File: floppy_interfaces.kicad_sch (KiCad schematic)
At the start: 24 parts, among them J13 Conn_01x04_Male, J14 Conn_02x17_Odd_Even, J16 Conn_01x04_Male, J6 SDF-60J for IEC 1541 serial p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, U1 74HC245, U2 74HC245, U22 74LS06N, U3 74HC245

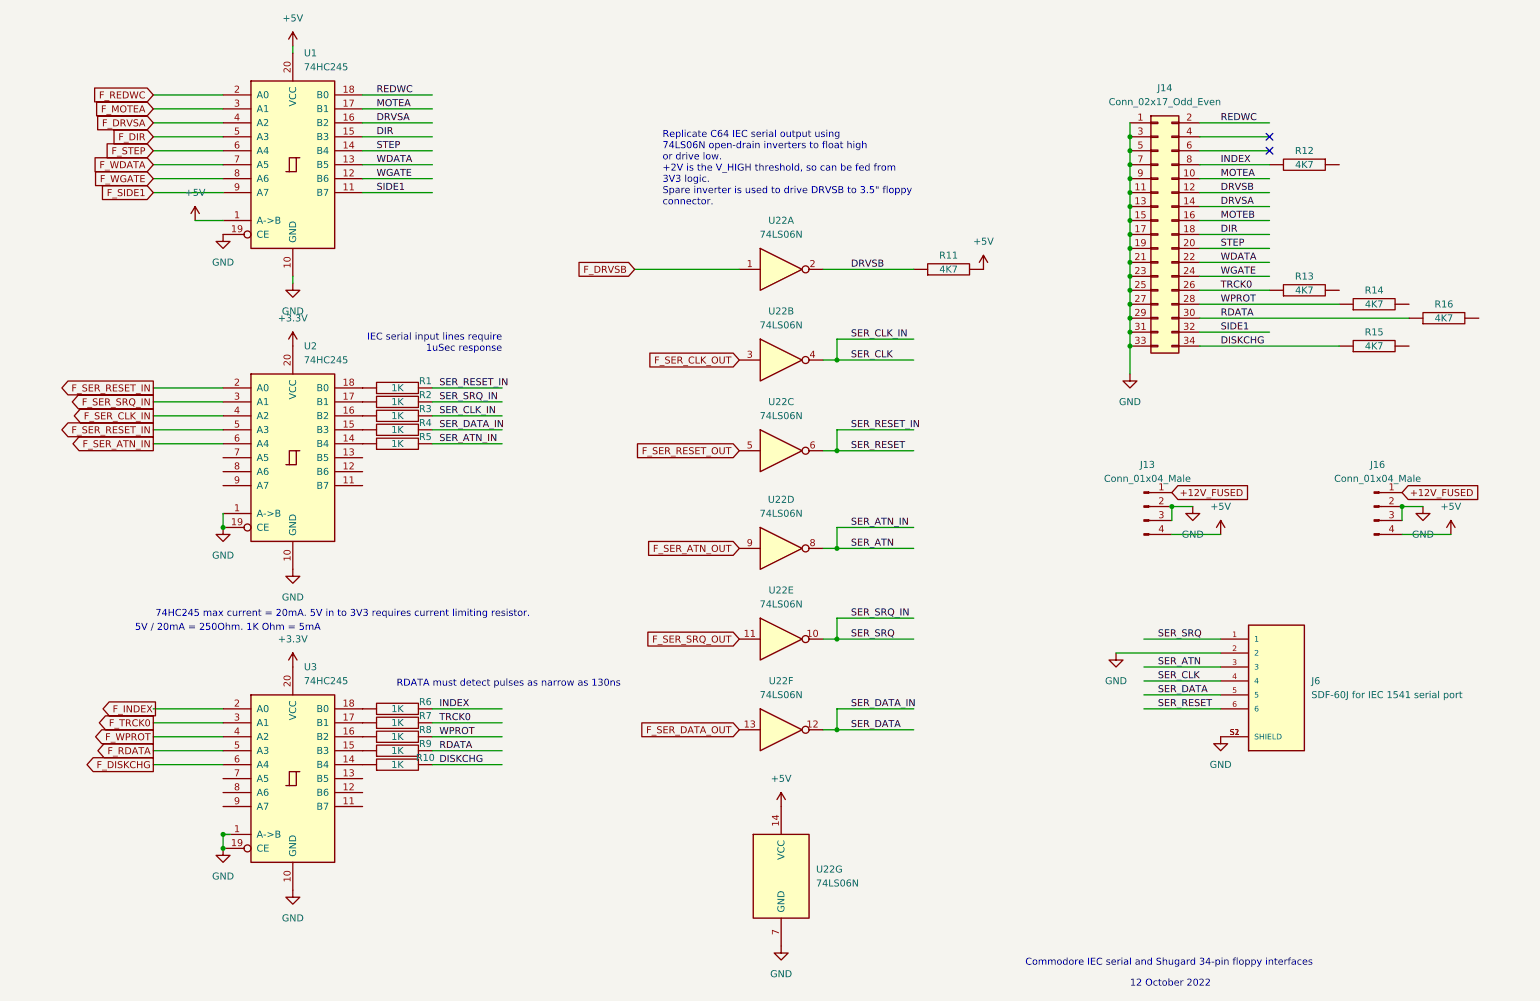
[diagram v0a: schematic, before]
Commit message: rework floppy buffers to use mux bus
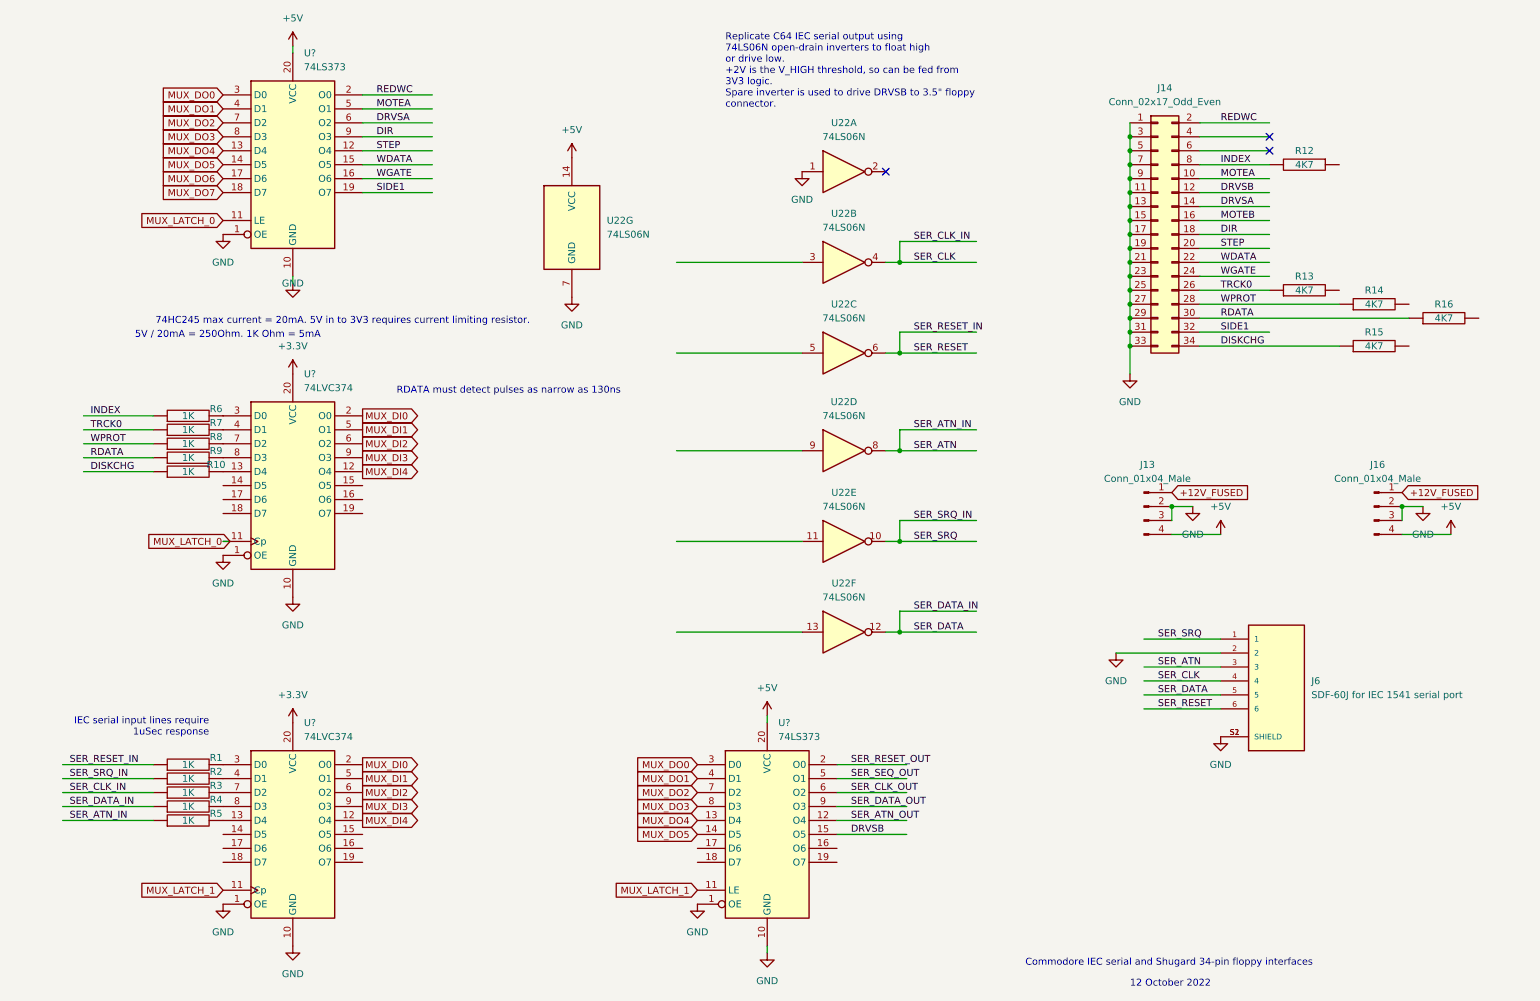
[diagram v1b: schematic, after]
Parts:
- removed R11: 4K7, Resistor_THT:R_Box_L8.4mm_W2.5mm_P5.08mm, symbol pspice:R
- removed U1, U2, U3: 74HC245, Package_DIP:DIP-20_W7.62mm, symbol 74xx:74HC245
- added U? (x2): 74LS373, symbol 74xx:74LS373
- added U? (x2): 74LVC374, Package_DIP:DIP-20_W7.62mm, symbol 74xx:74HC374
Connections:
- net F_DRVSB is gone; now on net GND: U22.1
- net +3V3: now also U?.20 (VCC), U?.20 (VCC)
- net +5V: now also U?.20 (VCC), U?.20 (VCC)
- net DIR: now also U?.9 (O3)
- net DISKCHG: now also R10.1; no longer R10.2
- net DRVSA: now also U?.6 (O2)
- net DRVSB: now also U?.15 (O5); no longer U22.2
- net GND: now also U?.1 (OE), U?.1 (OE), U?.1 (OE), U?.1 (OE), U?.10 (GND), U?.10 (GND), U?.10 (GND), U?.10 (GND)
- net INDEX: now also R6.1; no longer R6.2
- net MOTEA: now also U?.5 (O1)
- net RDATA: now also R9.1; no longer R9.2
- net REDWC: now also U?.2 (O0)
- net SER_ATN: now also R5.1; no longer R5.2
- net SER_CLK: now also R3.1; no longer R3.2
- net SER_DATA: now also R4.1; no longer R4.2
- net SER_RESET: now also R1.1; no longer R1.2
- net SER_SRQ: now also R2.1; no longer R2.2
- net SIDE1: now also U?.19 (O7)
- net STEP: now also U?.12 (O4)
- net TRCK0: now also R7.1; no longer R7.2
- net WDATA: now also U?.15 (O5)
- net WGATE: now also U?.16 (O6)
- net WPROT: now also R8.1; no longer R8.2
- net F_SER_ATN_OUT: no longer names the net of U22.9
- net F_SER_CLK_OUT: no longer names the net of U22.3
- net F_SER_DATA_OUT: no longer names the net of U22.13
- net F_SER_RESET_OUT: no longer names the net of U22.5
- net F_SER_SRQ_OUT: no longer names the net of U22.11
- new net: R2.2, U?.4 (D1)
- new net: R8.2, U?.7 (D2)
- new net: R7.2, U?.4 (D1)
- new net: R1.2, U?.3 (D0)
- new net: R5.2, U?.13 (D4)
- new net: R3.2, U?.7 (D2)
- new net: R4.2, U?.8 (D3)
- new net: R9.2, U?.8 (D3)
- new net: R10.2, U?.13 (D4)
- new net: R6.2, U?.3 (D0)
- new net MUX_DI0: U?.2 (O0), U?.2 (O0)
- new net MUX_DI1: U?.5 (O1), U?.5 (O1)
- new net MUX_DI2: U?.6 (O2), U?.6 (O2)
- new net MUX_DI3: U?.9 (O3), U?.9 (O3)
- new net MUX_DI4: U?.12 (O4), U?.12 (O4)
- new net MUX_DO0: U?.3 (D0), U?.3 (D0)
- new net MUX_DO1: U?.4 (D1), U?.4 (D1)
- new net MUX_DO2: U?.7 (D2), U?.7 (D2)
- new net MUX_DO3: U?.8 (D3), U?.8 (D3)
- new net MUX_DO4: U?.13 (D4), U?.13 (D4)
- new net MUX_DO5: U?.14 (D5), U?.14 (D5)
- new net MUX_DO6: U?.17 (D6)
- new net MUX_DO7: U?.18 (D7)
- new net MUX_LATCH_0: U?.11 (Cp), U?.11 (LE)
- new net MUX_LATCH_1: U?.11 (Cp), U?.11 (LE)
- new net SER_ATN_OUT: U?.12 (O4)
- new net SER_CLK_OUT: U?.6 (O2)
- new net SER_DATA_OUT: U?.9 (O3)
- new net SER_RESET_OUT: U?.2 (O0)
- new net SER_SEQ_OUT: U?.5 (O1)
- no-connect marks 2 -> 3
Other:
- moved on the sheet: R1, R10, R2, R3, R4, R5, R6, R7, R8, R9, U22A, U22B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

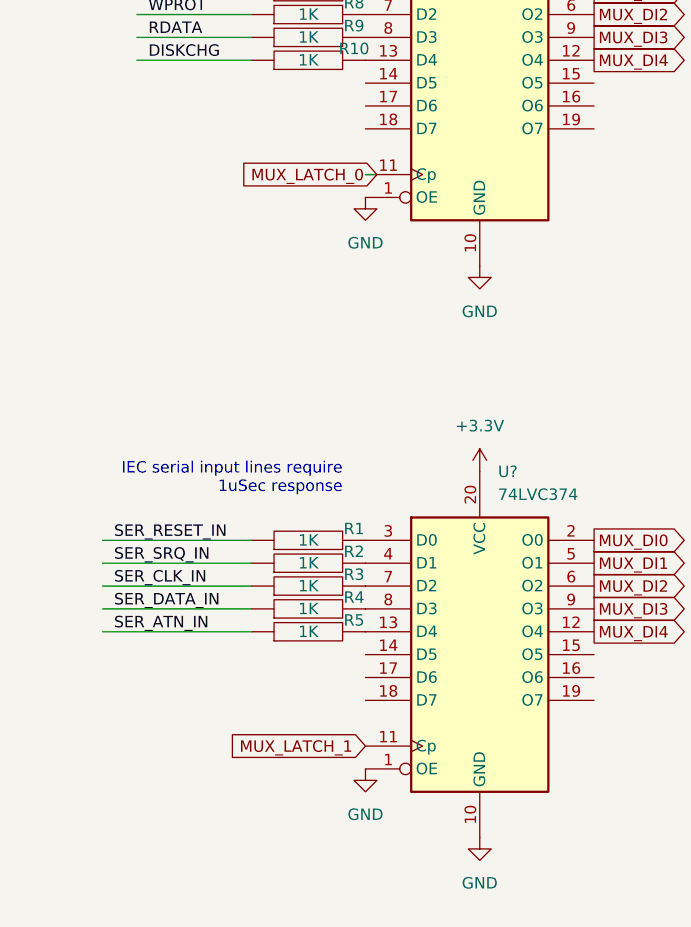
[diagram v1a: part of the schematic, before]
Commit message: add inverting mux to allow use of 74LVC374 as tristate buffer
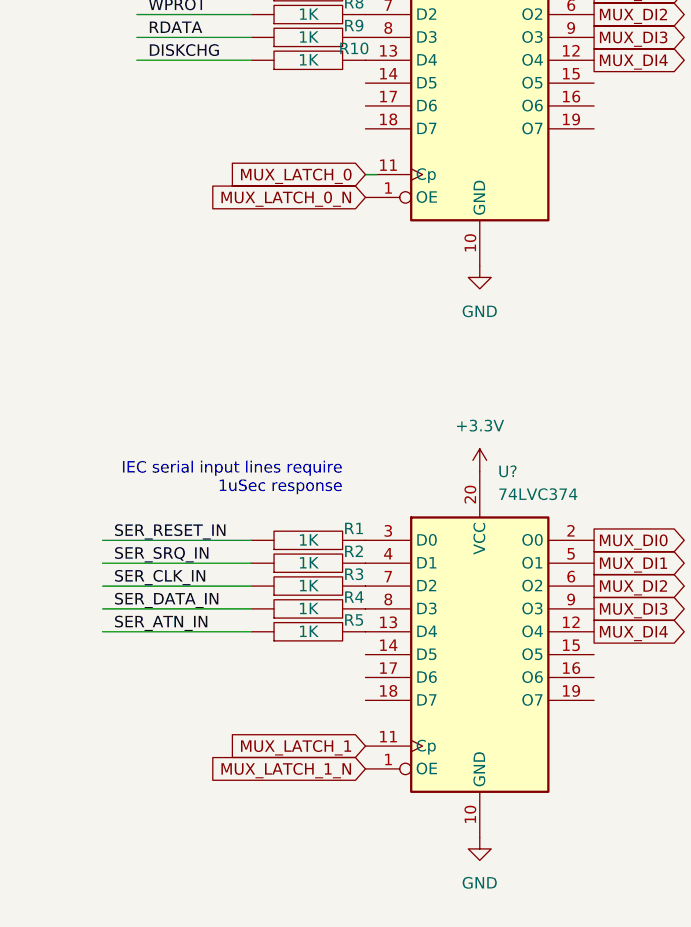
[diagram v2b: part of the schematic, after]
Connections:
- net GND: no longer U?.1 (OE), U?.1 (OE)
- new net MUX_LATCH_0_N: U?.1 (OE)
- new net MUX_LATCH_1_N: U?.1 (OE)
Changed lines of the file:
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@@
     )
   )
-  (global_label "MUX_LATCH_0" (shape input) (at 45.72 113.03 180) (fields_autoplaced)
-    (effects (font (size 1.27 1.27)) (justify right))
-    (property "Intersheet References" "${INTERSHEET_REFS}" (id 0) (at 30.4859 112.9506 0)
+  (global_label "MUX_LATCH_0" (shape input) (at 44.45 113.03 180) (fields_autoplaced)
+    (effects (font (size 1.27 1.27)) (justify right))
+    (property "Intersheet References" "${INTERSHEET_REFS}" (id 0) (at 29.2159 112.9506 0)
       (effects (font (size 1.27 1.27)) (justify right) hide)
     )
@@
     )
   )
+  (global_label "MUX_LATCH_0_N" (shape input) (at 44.45 115.57 180) (fields_autoplaced)
+    (effects (font (size 1.27 1.27)) (justify right))
+    (property "Intersheet References" "${INTERSHEET_REFS}" (id 0) (at 26.9179 115.4906 0)
+      (effects (font (size 1.27 1.27)) (justify right) hide)
+    )
+  )
   (global_label "MUX_DI3" (shape output) (at 69.85 161.29 0) (fields_autoplaced)
     (effects (font (size 1.27 1.27)) (justify left))
@@
     (effects (font (size 1.27 1.27)) (justify right))
     (property "Intersheet References" "${INTERSHEET_REFS}" (id 0) (at 33.2679 36.7506 0)
+      (effects (font (size 1.27 1.27)) (justify right) hide)
+    )
+  )
+  (global_label "MUX_LATCH_1_N" (shape input) (at 44.45 179.07 180) (fields_autoplaced)
+    (effects (font (size 1.27 1.27)) (justify right))
+    (property "Intersheet References" "${INTERSHEET_REFS}" (id 0) (at 26.9179 178.9906 0)
       (effects (font (size 1.27 1.27)) (justify right) hide)
     )
@@
     (pin "2")
   )
-  (symbol (lib_id "power:GND") (at 44.45 115.57 0) (unit 1)
-    (in_bom yes) (on_board yes) (fields_autoplaced)
-    (property "Reference" "#PWR0117" (id 0) (at 44.45 121.92 0)
-      (effects (font (size 1.27 1.27)) hide)
-    )
-    (property "Value" "GND" (id 1) (at 44.45 120.65 0))
-    (property "Footprint" "" (id 2) (at 44.45 115.57 0)
-      (effects (font (size 1.27 1.27)) hide)
-    )
-    (property "Datasheet" "" (id 3) (at 44.45 115.57 0)
-      (effects (font (size 1.27 1.27)) hide)
-    )
-    (pin "1")
-  )
-  (symbol (lib_id "power:GND") (at 44.45 179.07 0) (unit 1)
-    (in_bom yes) (on_board yes) (fields_autoplaced)
-    (property "Reference" "#PWR0120" (id 0) (at 44.45 185.42 0)
-      (effects (font (size 1.27 1.27)) hide)
-    )
-    (property "Value" "GND" (id 1) (at 44.45 184.15 0))
-    (property "Footprint" "" (id 2) (at 44.45 179.07 0)
-      (effects (font (size 1.27 1.27)) hide)
-    )
-    (property "Datasheet" "" (id 3) (at 44.45 179.07 0)
-      (effects (font (size 1.27 1.27)) hide)
-    )
-    (pin "1")
-  )
   (symbol (lib_id "74xx:74HC374") (at 57.15 166.37 0) (unit 1)
